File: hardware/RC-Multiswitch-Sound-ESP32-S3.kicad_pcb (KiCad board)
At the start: 2 copper layers, 41 parts, among them CN1 UART A, CN2 12V, CN3 TPA3116D2, J1 Ausgaenge, J2 PCM5102A, J3 MAX98357A, J4 GAIN, J5 UART B, J6 UART C, J7 Setup, J8 SD-VCC, J9 microSD-TF-Modul, U1 ESP32-S3-DevKitC-1 (N16R8), U2 ULN2803A

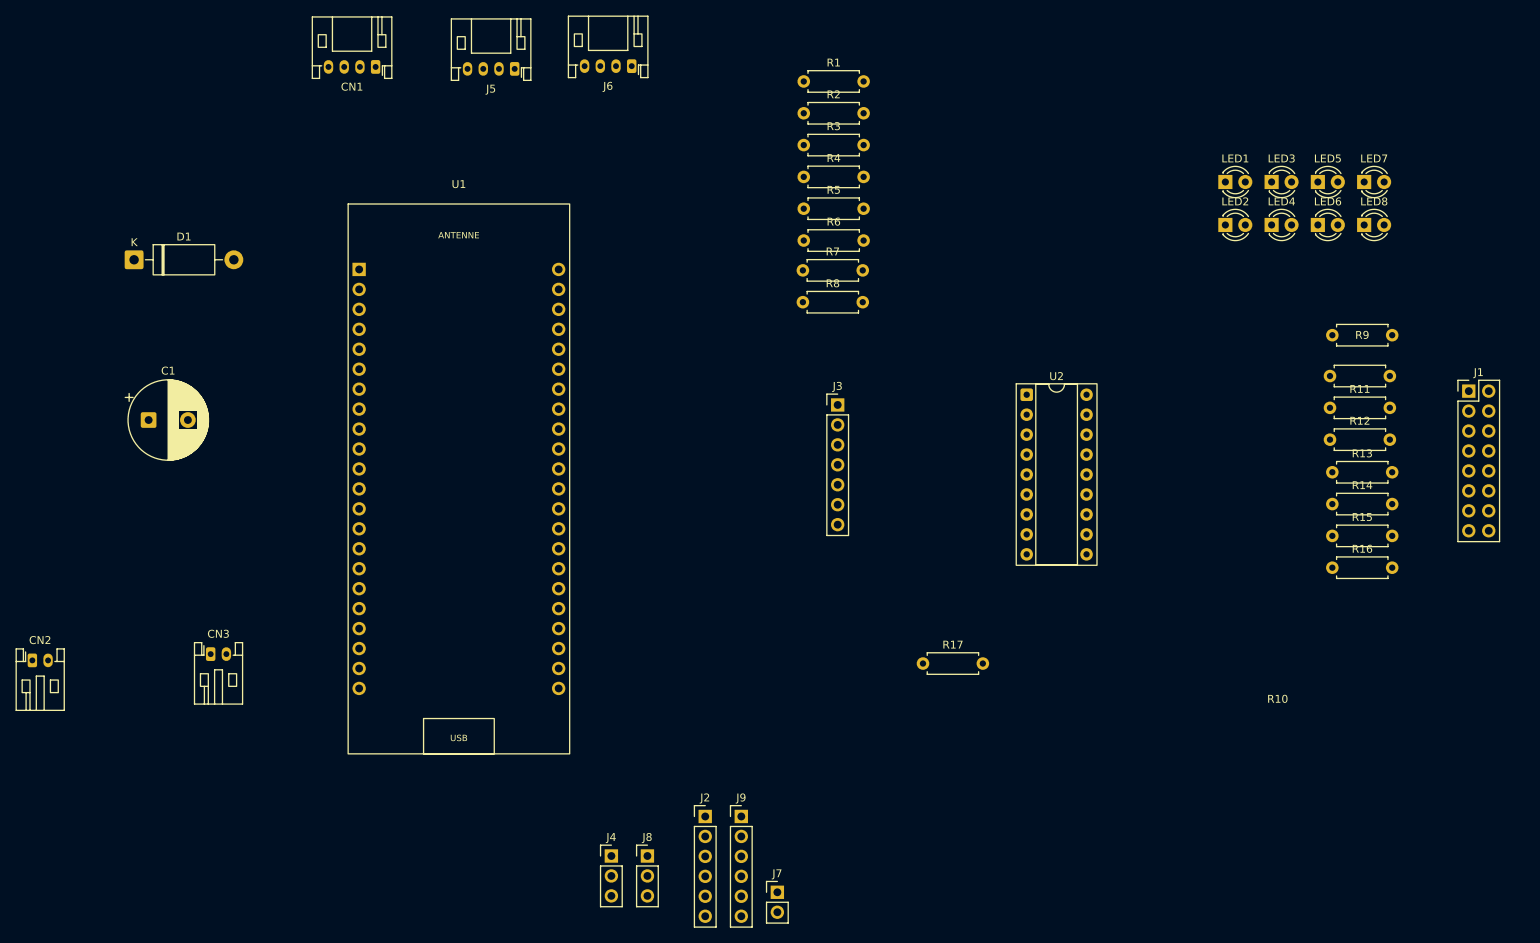
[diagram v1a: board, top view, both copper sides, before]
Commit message: Lokale KiCad-Staende vom 2026-10-17/18 uebernehmen
Die Arbeit lag nur lokal (nicht auf GitHub) und wurde beim Abgleich
nach der Umbenennung ueberschrieben. Wiederhergestellt aus
backups/vor-umbenennung, Dateinamen und Projektverweise auf
RC-Multiswitch angepasst.

Co-Authored-By: Claude Opus 5.5 (1M context) <noreply@anthropic.com>
Claude-Session: https://claude.ai/code/session_01Np9GkYmRMGJmd89YiKPa21
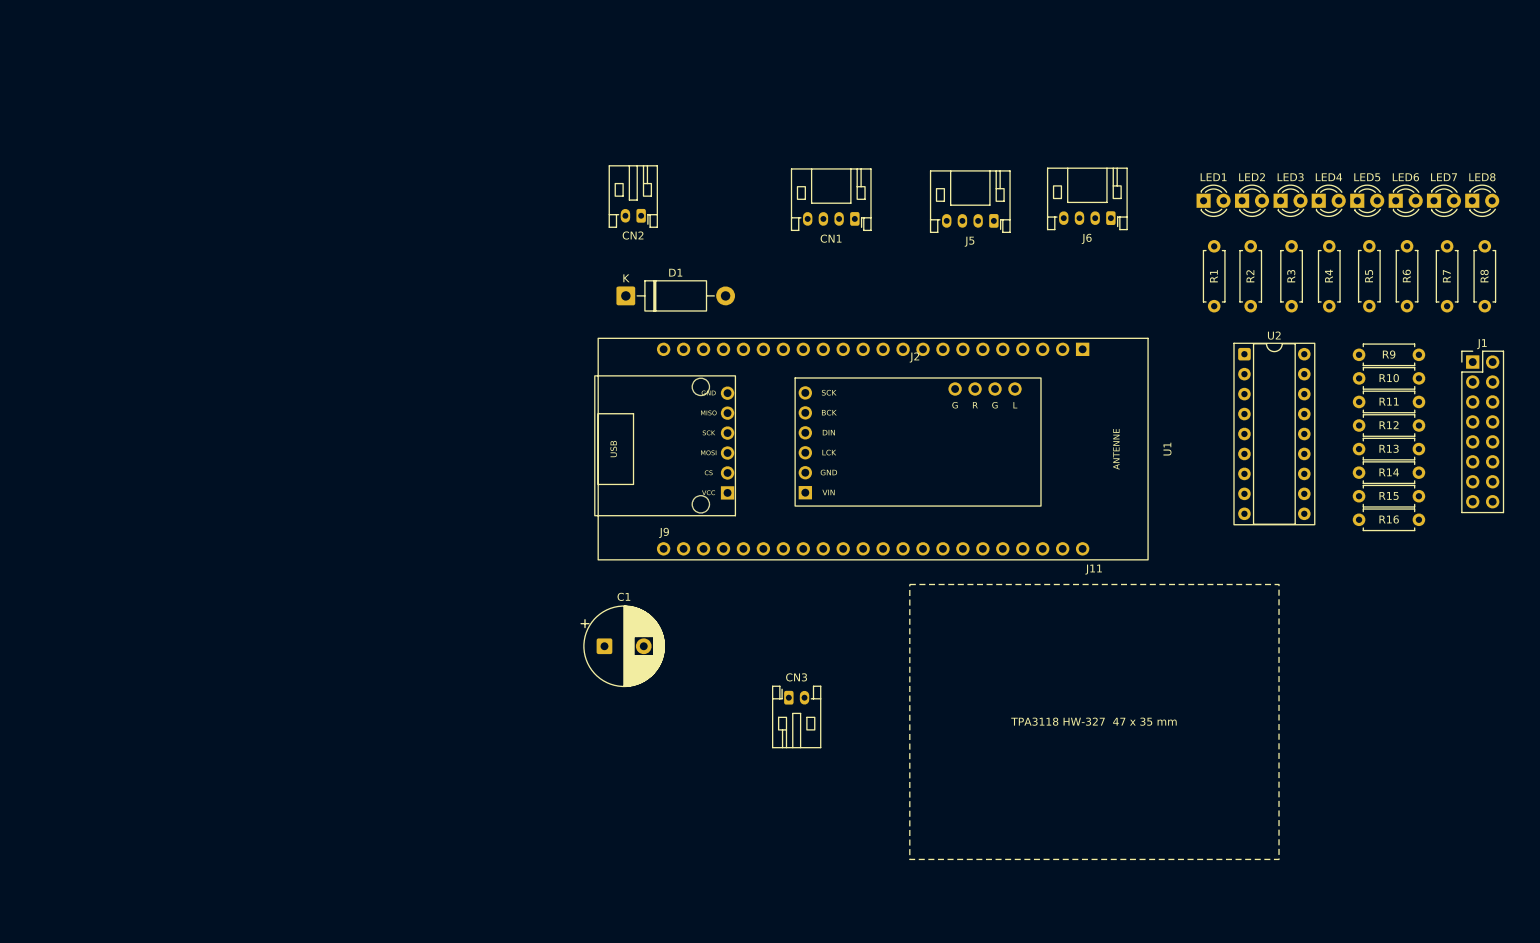
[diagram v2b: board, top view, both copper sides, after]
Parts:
- removed J3: MAX98357A, Connector_PinHeader_2.54mm:PinHeader_1x07_P2.54mm_Vertical
- removed J4: GAIN, Connector_PinHeader_2.54mm:PinHeader_1x03_P2.54mm_Vertical
- removed J7: Setup, Connector_PinHeader_2.54mm:PinHeader_1x02_P2.54mm_Vertical
- removed J8: SD-VCC, Connector_PinHeader_2.54mm:PinHeader_1x03_P2.54mm_Vertical
- removed R17: 100k, Resistor_THT:R_Axial_DIN0207_L6.3mm_D2.5mm_P7.62mm_Horizontal
- added J11: TPA3118 IN, ESP32-S3-DevKitC-1_THT:Mod_TPA3118_HW327_Keepout, F.Cu at (215.1, 129.5)
- CN3: value TPA3116D2 -> TPA3118
- J2: footprint Connector_PinHeader_2.54mm:PinHeader_1x06_P2.54mm_Vertical -> ESP32-S3-DevKitC-1_THT:Mod_PCM5102A_GY_THT
- J9: footprint Connector_PinHeader_2.54mm:PinHeader_1x06_P2.54mm_Vertical -> ESP32-S3-DevKitC-1_THT:Mod_microSD_SPI_THT
- moved CN2 96.0 mm to (157.4, 65.1), turned to 180 degrees
- moved R8 86.8 mm to (264.8, 76.6), turned to 90 degrees
- moved R7 82.1 mm to (260.0, 76.6), turned to 90 degrees
- moved R6 77.3 mm to (254.9, 76.6), turned to 90 degrees
- moved CN3 73.8 mm to (176.2, 126.5)
- moved R5 73.1 mm to (250.1, 76.6), turned to 90 degrees
- moved R4 68.9 mm to (245.0, 76.6), turned to 90 degrees
- moved R3 65.4 mm to (240.2, 76.6), turned to 90 degrees
- moved C1 64.8 mm to (152.7, 119.9)
- moved CN1 64.0 mm to (184.6, 65.5)
- moved J5 64.0 mm to (202.3, 65.8)
- moved J6 64.0 mm to (217.2, 65.4)
- moved D1 62.8 mm to (155.4, 75.3)
- moved R2 62.0 mm to (235.0, 76.6), turned to 90 degrees
- moved R1 59.6 mm to (230.3, 76.6), turned to 90 degrees
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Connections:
- J9 pad 1: /SD_VCC -> +3V3
- U1 pad 12: /AMP_SD -> unconnected-(U1-IO8-Pad12)
- U1 pad 15: /SETUP -> unconnected-(U1-IO9-Pad15)

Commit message: Widerstandswerte R1-R16 entfernt, Anwender legt sie aus
- R1-R16 ohne Wert (Schaltplan + PCB), Hinweis im Schaltplan angepasst
- Projektbeschreibung, README, README-hardware: Anwender legt Werte selbst aus, LED-Empfehlung im Schaltplan
- D1 P6KE15A und 3S-Versorgung bleiben (TPA3118 braucht >= 8 V)

Co-Authored-By: Claude Opus 5.5 (1M context) <noreply@anthropic.com>
Claude-Session: https://claude.ai/code/session_015ZTAHN4h1MhX6WfGWCfmx3
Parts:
- R1, R10, R11, R12, R13, R14, R15, R16, R2, R3, R4, R5, R6, R7, R8, R9: value 150 -> R
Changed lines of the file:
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@@
 			)
 		)
-		(property "Value" "150"
+		(property "Value" "R"
 			(at 3.81 3.02 90)
 			(layer "F.Fab")
@@
 			)
 		)
-		(property "Value" "150"
+		(property "Value" "R"
 			(at 3.81 3.12 90)
 			(layer "F.Fab")
@@
 			)
 		)
-		(property "Value" "150"
+		(property "Value" "R"
 			(at 3.81 2.37 0)
 			(layer "F.Fab")
@@
 			)
 		)
-		(property "Value" "150"
+		(property "Value" "R"
 			(at 3.81 2.97 90)
 			(layer "F.Fab")
@@
 			)
 		)
-		(property "Value" "150"
+		(property "Value" "R"
 			(at 3.81 3.12 90)
 			(layer "F.Fab")
@@
 			)
 		)
-		(property "Value" "150"
+		(property "Value" "R"
 			(at 3.81 2.37 0)
 			(layer "F.Fab")
@@
 			)
 		)
-		(property "Value" "150"
+		(property "Value" "R"
 			(at 3.81 2.37 0)
 			(layer "F.Fab")
@@
 			)
 		)
-		(property "Value" "150"
+		(property "Value" "R"
 			(at 3.81 5.2 90)
 			(layer "F.Fab")
@@
 			)
 		)
-		(property "Value" "150"
+		(property "Value" "R"
 			(at 3.81 2.37 0)
 			(layer "F.Fab")
@@
 			)
 		)
-		(property "Value" "150"
+		(property "Value" "R"
 			(at 3.81 2.37 0)
 			(layer "F.Fab")
@@
 			)
 		)
-		(property "Value" "150"
+		(property "Value" "R"
 			(at 3.81 2.37 0)
 			(layer "F.Fab")
@@
 			)
 		)
-		(property "Value" "150"
+		(property "Value" "R"
 			(at 3.82 3.52 90)
 			(layer "F.Fab")
@@
 			)
 		)
-		(property "Value" "150"
+		(property "Value" "R"
 			(at 3.81 2.37 90)
 			(layer "F.Fab")
@@
 			)
 		)
-		(property "Value" "150"
+		(property "Value" "R"
 			(at 3.91 3.67 90)
 			(layer "F.Fab")
@@
 			)
 		)
-		(property "Value" "150"
+		(property "Value" "R"
 			(at 3.81 2.37 0)
 			(layer "F.Fab")
@@
 			)
 		)
-		(property "Value" "150"
+		(property "Value" "R"
 			(at 3.81 2.37 0)
 			(layer "F.Fab")

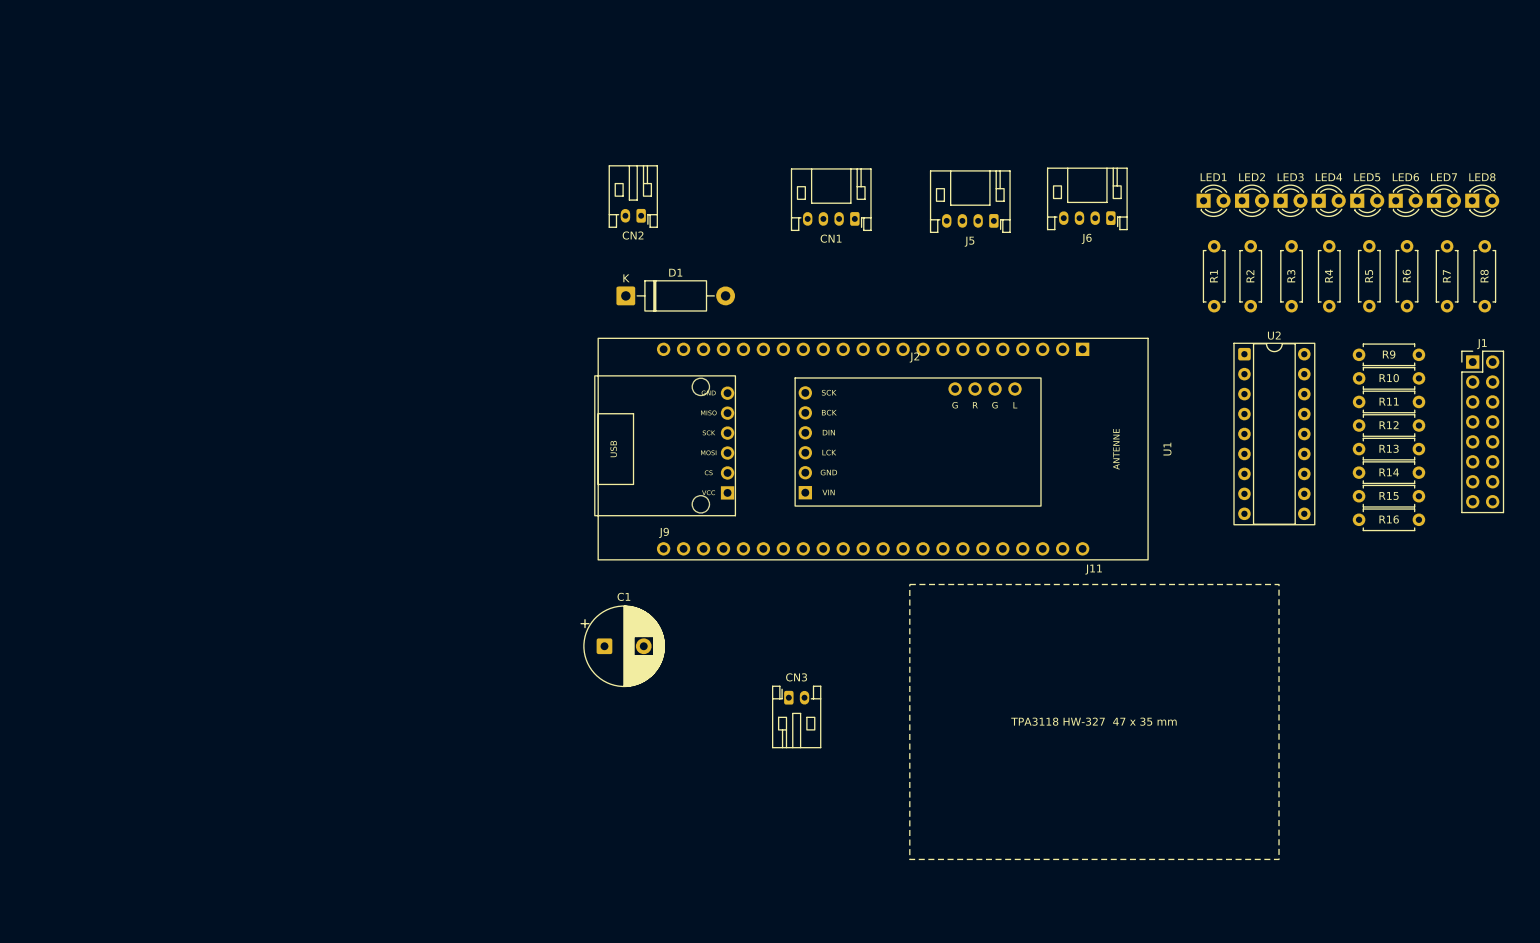
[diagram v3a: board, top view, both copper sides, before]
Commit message: PCB: Routing von Martins PC übernommen, VLOAD-Bahnen auf 0,4 mm
Übernimmt das lokal mit Freerouting geroutete Layout (Stand 18.10.2026
19:53) und setzt alle 28 Leiterbahn-Segmente des Netzes /VLOAD von
0,2 mm auf 0,4 mm Breite. Sonst unverändert, CRLF beibehalten.

Co-Authored-By: Claude Opus 5.5 (1M context) <noreply@anthropic.com>
Claude-Session: https://claude.ai/code/session_018bh1aktNNbeTvdMLiwxhbB
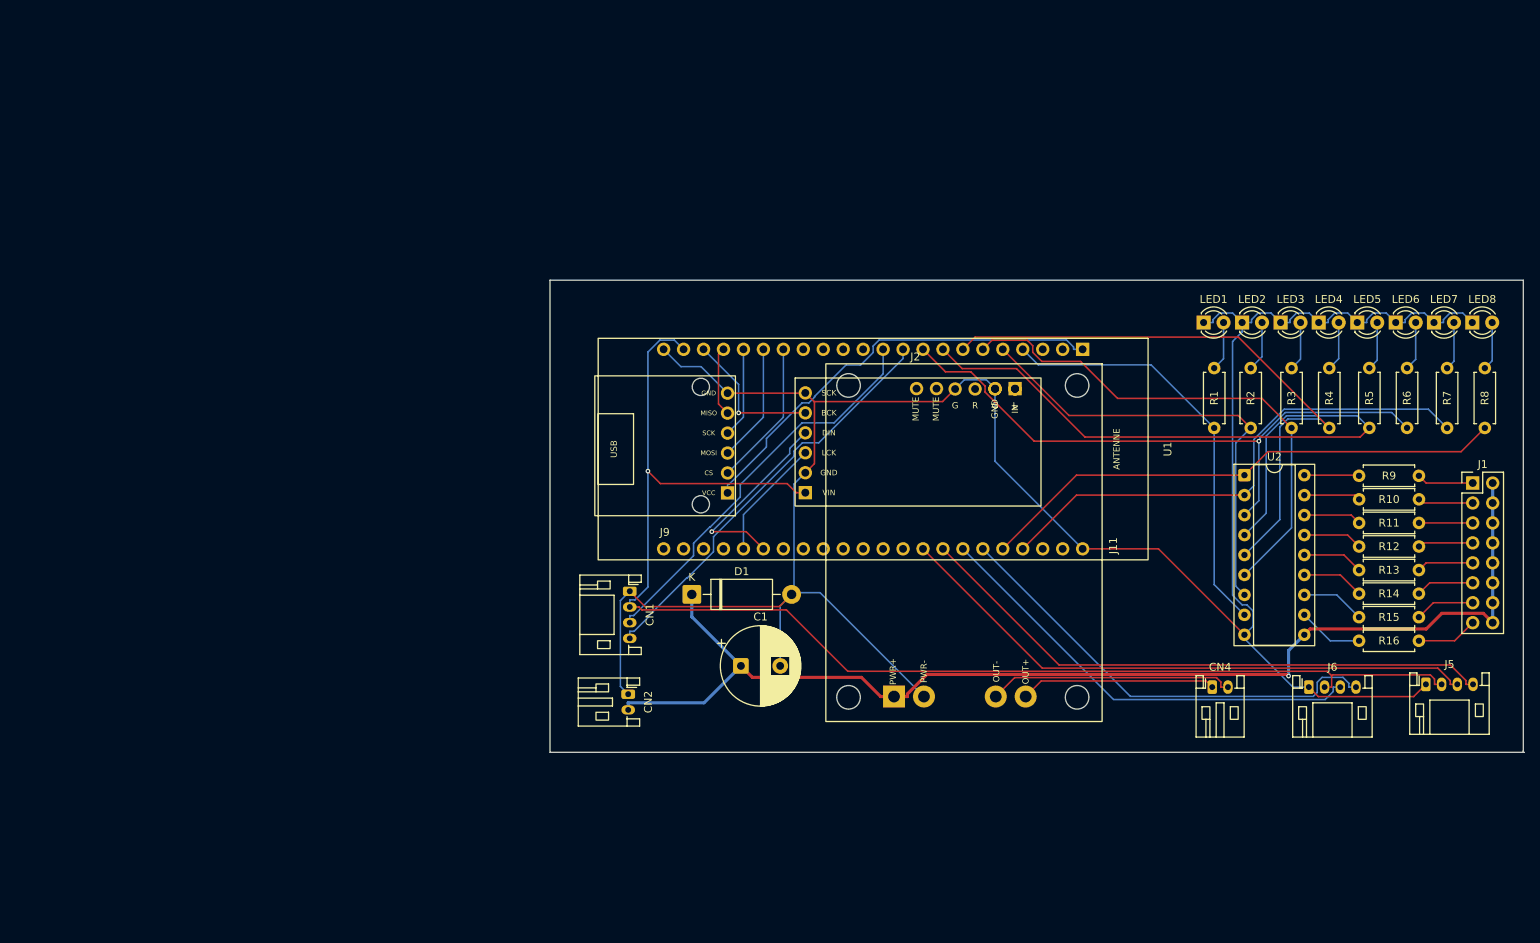
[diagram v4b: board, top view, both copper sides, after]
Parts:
- removed CN3: TPA3118, Connector_JST:JST_PH_S2B-PH-K_1x02_P2.00mm_Horizontal
- added CN4: Lautsprecher, Connector_JST:JST_PH_S2B-PH-K_1x02_P2.00mm_Horizontal, F.Cu at (230.1, 125.1)
- CN2: value 12V -> 3S
- D1: value P6KE33A -> P6KE15A
- J11: value TPA3118 IN -> TPA3118 HW-327; footprint ESP32-S3-DevKitC-1_THT:Mod_TPA3118_HW327_Keepout -> ESP32-S3-DevKitC-1_THT:Mod_TPA3118_HW327_THT
- moved J5 80.7 mm to (257.3, 124.8), turned to 0 degrees
- moved J6 64.8 mm to (242.4, 125.1), turned to 0 degrees
- moved CN2 60.9 mm to (155.8, 126.0), turned to -90 degrees
- moved CN1 55.4 mm to (155.9, 112.9), turned to -90 degrees
- moved J11 43.6 mm to (205.0, 87.1), turned to -90 degrees
- moved D1 38.9 mm to (163.8, 113.3)
- moved C1 17.5 mm to (170.1, 122.4)
- moved LED1 15.5 mm to (229.0, 78.7)
- moved LED2 15.5 mm to (233.9, 78.7)
- moved LED3 15.5 mm to (238.8, 78.7)
- moved LED4 15.5 mm to (243.7, 78.7)
- moved LED5 15.5 mm to (248.6, 78.7)
- moved LED6 15.5 mm to (253.5, 78.7)
- moved LED7 15.5 mm to (258.3, 78.7)
- moved LED8 15.5 mm to (263.2, 78.7)
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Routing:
- net GND: track 0.00 -> 302.5 mm
- net +5V: track 0.00 -> 170.9 mm, vias 0 -> 1
- net /VLOAD: track 0.00 -> 151.1 mm, vias 0 -> 1
- net /S4: track 0.00 -> 88.0 mm
- net /S5: track 0.00 -> 79.6 mm, vias 0 -> 1
- net /S3: track 0.00 -> 77.4 mm
- net /UB_TX: track 0.00 -> 75.5 mm
- net /UB_RX: track 0.00 -> 74.9 mm
- net /S7: track 0.00 -> 67.7 mm
- net /S2: track 0.00 -> 66.1 mm
- net /S6: track 0.00 -> 65.8 mm
- net /S1: track 0.00 -> 58.2 mm
- net /UC_RX: track 0.00 -> 57.9 mm
- net /UC_TX: track 0.00 -> 57.0 mm
- net +3V3: track 0.00 -> 55.8 mm
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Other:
- board outline added: 124 x 60.1 mm
